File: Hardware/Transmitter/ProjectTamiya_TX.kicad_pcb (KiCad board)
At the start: 2 copper layers, 106.2 x 40 mm, 43 parts, among them J1 Boot, J10 NRF, J11 NRF_power, J2 Power, J3 Serial, J4 Steering, J5 Throttle, J6 ENC1, J7 OLED, J8 ENC2, J9 Debug, Q1 2N7002A, Q2 2N7002A, Q3 2N7002A, SW1 Reset, SW2 Switch, U1 STM32F303CCT6, U2 AP2111H-3.3TRG1, Y1 XT324 [20pF, 12MHz]

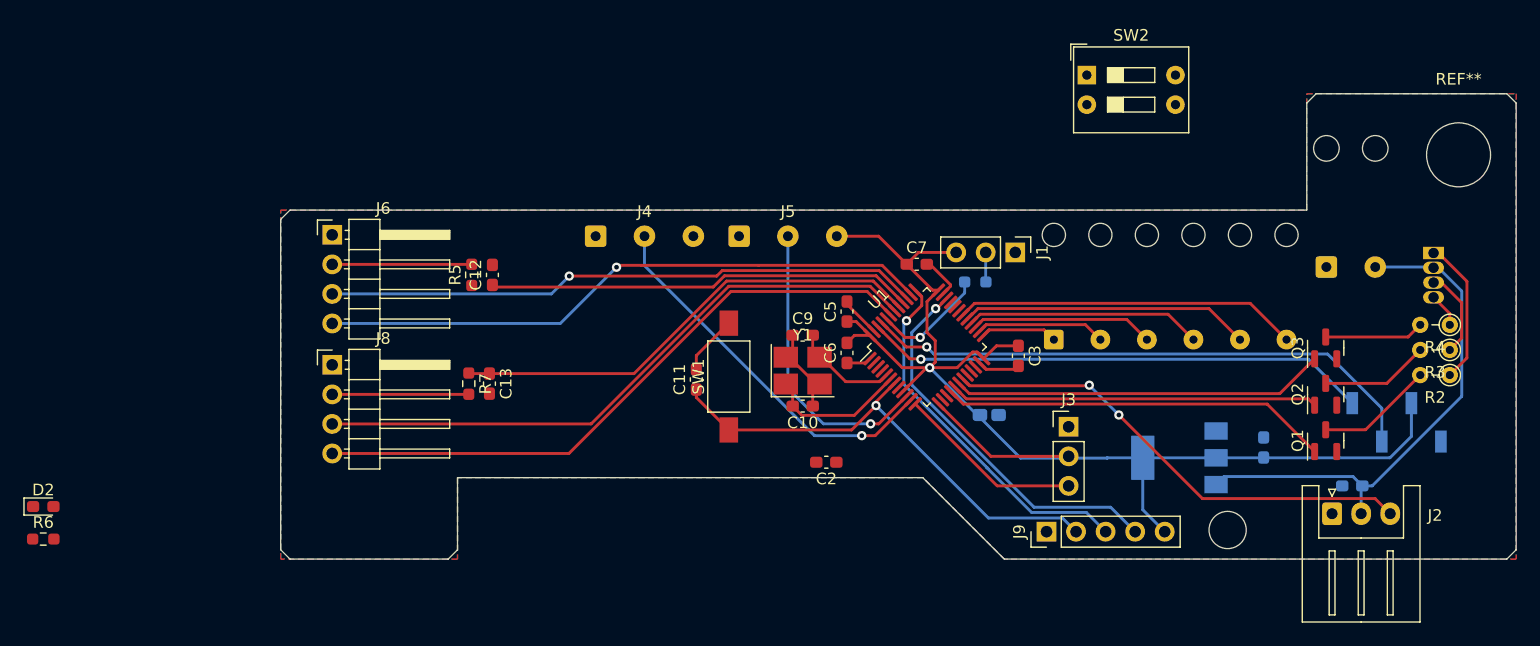
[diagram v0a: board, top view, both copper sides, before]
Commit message: Switch pin assignment change, updated schematics, complete PCB
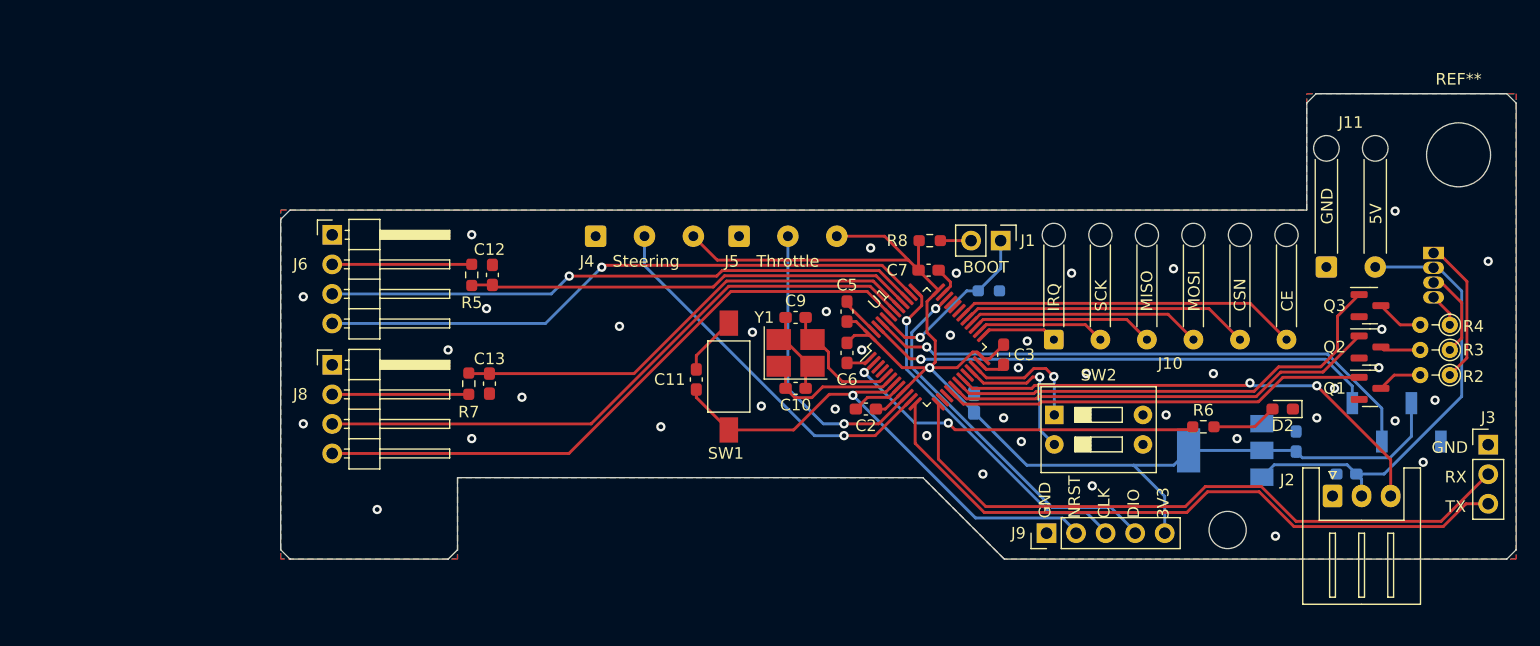
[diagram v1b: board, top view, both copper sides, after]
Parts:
- added R8: 1K, Resistor_SMD:R_0603_1608Metric_Pad0.98x0.95mm_HandSolder, F.Cu at (113.8, 55.6)
- J1: footprint Connector_PinHeader_2.54mm:PinHeader_1x03_P2.54mm_Vertical -> Connector_PinHeader_2.54mm:PinHeader_1x02_P2.54mm_Vertical
- moved D2 106.9 mm to (144.1, 70.1), turned to 180 degrees
- moved R6 100.2 mm to (137.3, 71.6)
- moved J3 36.1 mm to (161.8, 73.2)
- moved SW2 29.3 mm to (124.5, 70.6)
- moved Q1 5.89 mm to (151.6, 68.3), turned to 0 degrees
- moved C2 5.70 mm to (108.3, 70.1)
- moved Q2 5.57 mm to (151.6, 64.8), turned to 0 degrees
- moved Q3 5.27 mm to (151.6, 61.2), turned to 0 degrees
- moved U2 3.99 mm to (139.2, 73.7)
- moved C8 2.84 mm to (145.3, 72.9)
- moved C1 1.66 mm to (117.6, 69.6), turned to 90 degrees
- moved C10 1.64 mm to (102.3, 68.3)
- moved C9 1.64 mm to (102.3, 62.2)
- moved Y1 1.64 mm to (102.3, 65.3)
- moved J1 1.61 mm to (119.9, 55.6)
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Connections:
- J1 pad 1: GND -> Net-(J1-Pad1)
- R1 pad 1: Net-(J1-Pad2) -> GND
- R1 pad 2: Net-(R1-Pad2) -> Net-(J1-Pad1)
- U1 pad 21: SW1 -> SW2
- U1 pad 22: SW2 -> SW1
- U1 pad 44: Net-(R1-Pad2) -> Net-(J1-Pad1)
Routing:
- net USART2_RX: track 13.1 -> 57.3 mm
- net USART2_TX: track 16.1 -> 57.9 mm
- net LED1: track 0.00 -> 31.6 mm, vias 0 -> 2
- net +3V3: track 101.5 -> 120.7 mm
- net Net-(J1-Pad1): track 0.00 -> 15.3 mm, vias 0 -> 1
- net SW2: track 0.00 -> 12.9 mm, vias 0 -> 1
- net SW1: track 0.00 -> 11.1 mm, vias 0 -> 1
- net Net-(R1-Pad2): track 9.92 -> 0.00 mm, vias 1 -> 0
- net LED_B: track 32.2 -> 40.0 mm
- net Net-(Q1-Pad3): track 10.1 -> 3.85 mm
- net LED_G: track 31.6 -> 37.4 mm
- net Net-(Q2-Pad3): track 9.32 -> 3.49 mm
- net Net-(D2-Pad2): track 0.00 -> 5.66 mm
- net +5V: track 44.7 -> 40.1 mm
- net Net-(Q3-Pad3): track 8.56 -> 4.06 mm
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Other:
- board text added: "3V3"
- board text added: "5V"
- board text added: "BOOT"
- board text added: "CE"
- board text added: "CLK"
- board text added: "CSN"
- board text added: "DIO"
- board text added: "GND"
- board text added: "IRQ"
- board text added: "MISO"
- board text added: "MOSI"
- board text added: "NRST"
- board text added: "RX"
- board text added: "SCK"
- board text added: "Steering"
- board text added: "TX"
- board text added: "Throttle"

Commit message: Rerouted tracks to have bigger spaces and other adjustments
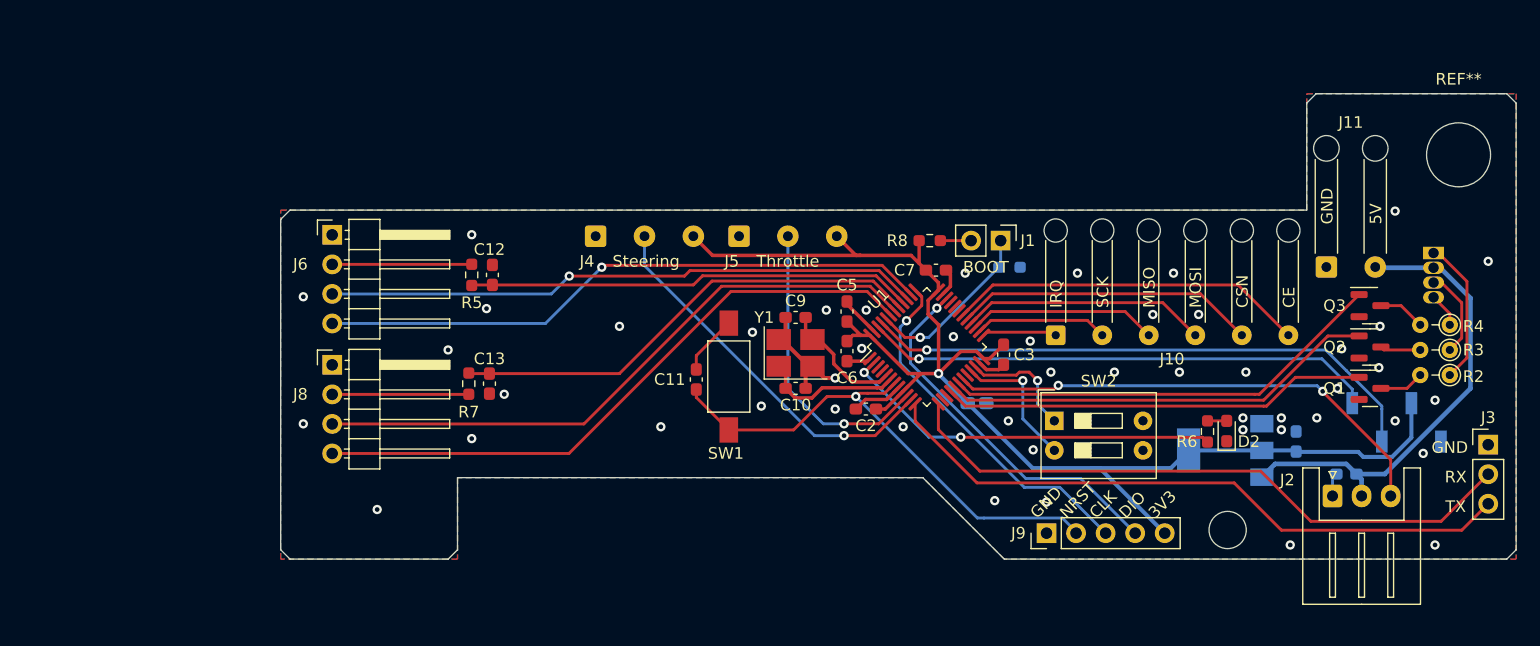
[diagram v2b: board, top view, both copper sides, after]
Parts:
- moved D2 5.17 mm to (139.3, 72.0), turned to 90 degrees
- moved R1 2.70 mm to (120.7, 57.9)
- moved C7 0.63 mm to (114.3, 58.2)
- moved R6 0.54 mm to (137.7, 72.0), turned to 90 degrees
- moved SW2 0.51 mm to (124.5, 71.1)
- moved J10 0.41 mm to (124.6, 63.8)
- moved C1 0.25 mm to (117.9, 69.6), turned to 0 degrees
- moved C6 0.15 mm to (106.7, 65.1)
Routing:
- net +3V3: track 120.7 -> 116.4 mm
- net GND: track 26.5 -> 30.6 mm, vias 41 -> 49
- net Net-(D2-Pad2): track 5.66 -> 1.65 mm
- net USART2_RX: track 57.3 -> 54.4 mm
- net USART2_TX: track 57.9 -> 55.6 mm
- net LED_B: track 40.0 -> 38.3 mm
- net LED1: track 31.6 -> 33.2 mm
- net NRF_CE: track 29.5 -> 30.8 mm
- net NRF_CSN: track 25.0 -> 26.0 mm
- net SW1: track 11.1 -> 10.1 mm
- net SW2: track 12.9 -> 11.9 mm
- net NRF_MOSI: track 20.3 -> 21.1 mm
- net +5V: track 40.1 -> 40.9 mm
- net SWDIO: track 31.5 -> 32.2 mm
- net NRF_MISO: track 15.7 -> 16.3 mm
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
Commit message: Routing adjustments, curved tracks
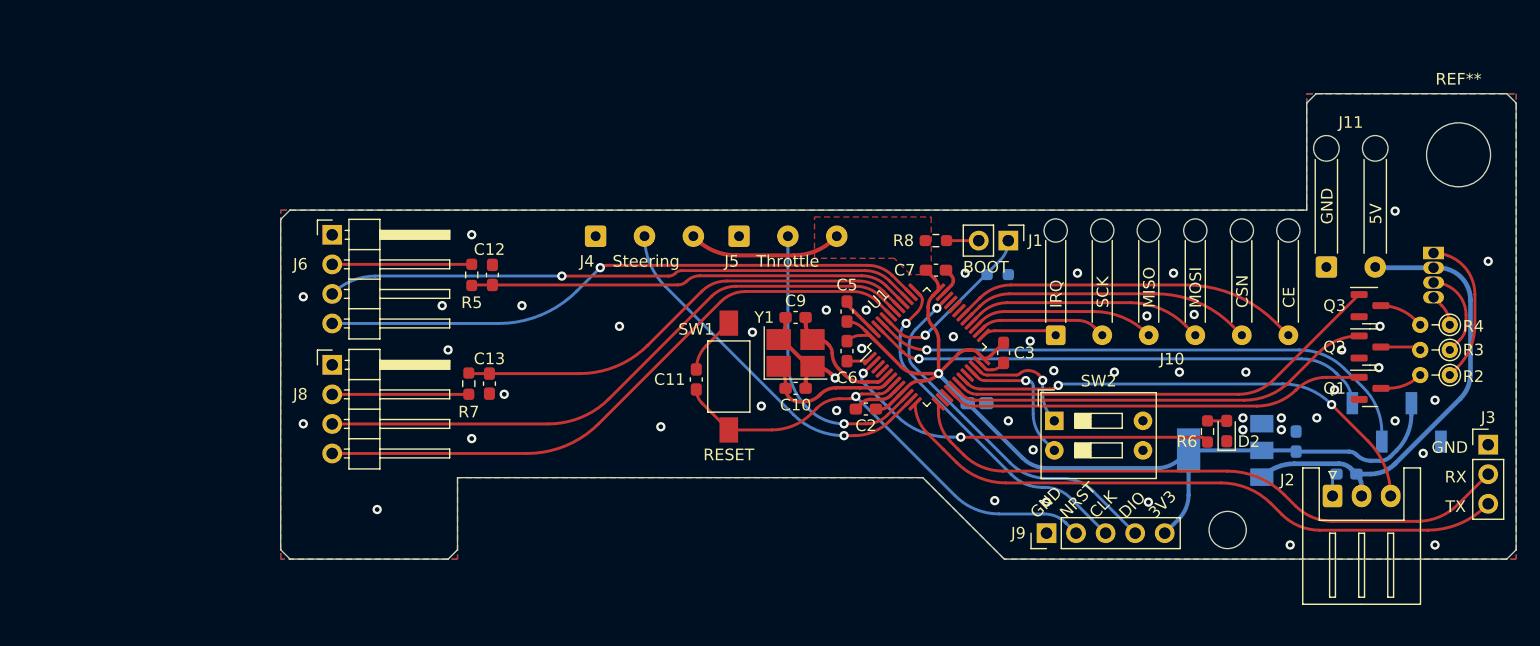
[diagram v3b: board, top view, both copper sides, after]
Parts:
- moved R1 1.20 mm to (119.6, 58.5)
- moved J1 0.66 mm to (120.5, 55.6)
- moved R8 0.53 mm to (114.3, 55.6)
- moved C3 0.15 mm to (120.1, 65.3)
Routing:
- net +3V3: track 116.4 -> 103.4 mm
- net USART2_TX: track 55.6 -> 54.3 mm
- net USART2_RX: track 54.4 -> 53.2 mm
- net NRST: track 44.3 -> 43.4 mm
- net STEERING: track 32.8 -> 32.0 mm
- net ENC2_CH2: track 54.6 -> 53.9 mm
- net NRF_CE: track 30.8 -> 30.1 mm
- net OLED_SCL: track 48.9 -> 48.2 mm
- net ENC2_BTN: track 41.2 -> 40.5 mm
- net ENC2_CH1: track 54.1 -> 53.5 mm
- net ENC1_CH1: track 52.9 -> 52.2 mm
- net NRF_CSN: track 26.0 -> 25.4 mm
- net THROTTLE: track 25.6 -> 25.0 mm
- net LED_G: track 37.5 -> 36.9 mm
- net SWCLK: track 31.0 -> 30.4 mm
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- added copper zone on F.Cu, net +3V3
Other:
- board text added: "RESET"
